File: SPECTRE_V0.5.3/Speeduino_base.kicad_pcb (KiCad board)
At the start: 2 copper layers, 100 x 93 mm, 218 parts, among them J1 Conn_01x06_Male, J2 Conn_02x04_Odd_Even, J3 ProtoArea, Q1 AO3400, Q10 BSP78, Q11 BSP78, Q12 AO3400, Q13 BSP78, Q14 BSP78, Q15 BSP78, Q16 BSP78, Q17 BSP78, Q18 BSP78, Q19 BSP78, Q20 BSP78, Q21 BSP78, Q6 AO3400, Q7 AO3400, U1 MAX9926UAEE+, U10 MIC4427, U2 LM78M05_TO220, U3 TL431DBZ, U4 molex_48pin, U5 TJA1050, U6 MAX3232, U7 MIC4427, U8 MIC4427, U9 MIC4427

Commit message: more cleanup after changing molex 48pin
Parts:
- U4: footprint rusefi_lib:Molex_48 -> Speeduino_base:Molex_48
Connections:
- JP13 pad 1: CANH -> Net-(JP13-Pad1)
- JP13 pad 2: Net-(JP13-Pad2) -> CANH
- R25 pad 1: PC2 -> Net-(C11-Pad2)
- R25 pad 2: Net-(C11-Pad2) -> PC2
- R28 pad 1: PC4 -> Net-(C14-Pad2)
- R28 pad 2: Net-(C14-Pad2) -> PC4
- R46 pad 1: PB1 -> Net-(C20-Pad2)
- R46 pad 2: Net-(C20-Pad2) -> PB1
- R66 pad 1: Net-(Q7-Pad1) -> PWR_GND
- R66 pad 2: PWR_GND -> Net-(Q7-Pad1)
- R67 pad 1: Net-(Q7-Pad1) -> PC13
- R67 pad 2: PC13 -> Net-(Q7-Pad1)
- R74 pad 1: Net-(JP13-Pad2) -> Net-(JP13-Pad1)
- R83 pad 1: PD3 -> PC7
- R86 pad 1: Net-(Q15-Pad1) -> PWR_GND
- R86 pad 2: PWR_GND -> Net-(Q15-Pad1)
- R87 pad 1: Net-(Q16-Pad1) -> PWR_GND
- R87 pad 2: PWR_GND -> Net-(Q16-Pad1)
- R88 pad 1: Net-(Q17-Pad1) -> PWR_GND
- R88 pad 2: PWR_GND -> Net-(Q17-Pad1)
- R9 pad 1: PA4 -> Net-(C3-Pad2)
- R9 pad 2: Net-(C3-Pad2) -> PA4
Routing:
- net PWR_GND: vias 98 -> 97
- net GND: vias 159 -> 158
- net (no net): vias 0 -> 2

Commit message: cleaning up board
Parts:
- moved D24 2.17 mm to (132.6, 101.6)
- moved R64 0.51 mm to (130.0, 102.6)
- moved JP15 0.25 mm to (163.1, 105.7)
- turned R66 to 180 degrees
- turned R67 to 0 degrees
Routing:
- net BOOT0_EXT: track 0.00 -> 48.9 mm, vias 0 -> 2
- net 3.3V: track 496.5 -> 508.9 mm
- net FLEX_FUEL_IN: track 0.00 -> 6.42 mm
- net Net-(JP15-Pad2): track 82.3 -> 87.9 mm
- net BOOT0: track 8.76 -> 13.0 mm
- net PE0: track 68.0 -> 70.4 mm
- net GND: track 706.9 -> 705.8 mm
- net Net-(D23-Pad3): track 44.6 -> 44.1 mm

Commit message: Done re-routing
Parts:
- moved R71 41.4 mm to (193.8, 46.2), turned to 90 degrees
- moved R70 41.2 mm to (196.6, 46.2), turned to 90 degrees
- moved R58 0.25 mm to (165.1, 77.5)
- turned JP13 to 180 degrees
- turned R25 to 0 degrees
- turned R28 to 180 degrees
- turned R46 to 90 degrees
- turned R86 to 180 degrees
- turned R87 to 0 degrees
- turned R88 to 0 degrees
- turned R9 to 270 degrees
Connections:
- R83 pad 1: PC7 -> PD3
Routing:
- net 3.3V: track 508.9 -> 525.6 mm, vias 14 -> 16
- net Spare_2-Out: track 25.4 -> 12.8 mm
- net Spare_1-Out: track 24.8 -> 13.6 mm
- net Net-(R70-Pad2): track 0.00 -> 10.8 mm
- net Net-(R71-Pad2): track 0.00 -> 8.02 mm
- net GND: track 705.8 -> 700.3 mm, vias 158 -> 159
- net PD3: track 36.4 -> 39.5 mm
- net Net-(JP13-Pad1): track 0.00 -> 2.00 mm
- net Net-(JP13-Pad2): track 1.99 -> 0.00 mm
- net PA10: track 73.0 -> 71.4 mm
- net PE1: track 85.0 -> 85.8 mm
- net Net-(R58-Pad2): track 3.95 -> 4.70 mm
- net IGN4-OUT: track 36.0 -> 36.6 mm
- net PWR_GND: vias 97 -> 99

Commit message: Clean-up board
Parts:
- moved JP15 2.29 mm to (165.4, 105.7)
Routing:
- net FLEX_FUEL_IN: track 6.42 -> 11.6 mm
- net Net-(JP15-Pad2): track 87.9 -> 90.8 mm
- net BOOT0_EXT: track 48.9 -> 50.8 mm
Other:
- board text removed: "BOOT1"

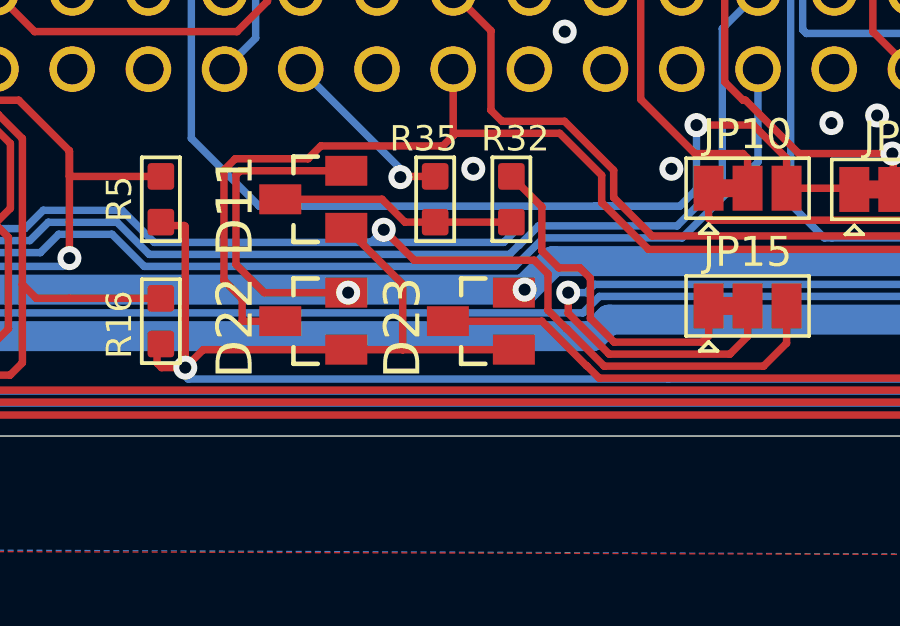
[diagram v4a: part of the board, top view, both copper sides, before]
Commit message: Update Canbus interface
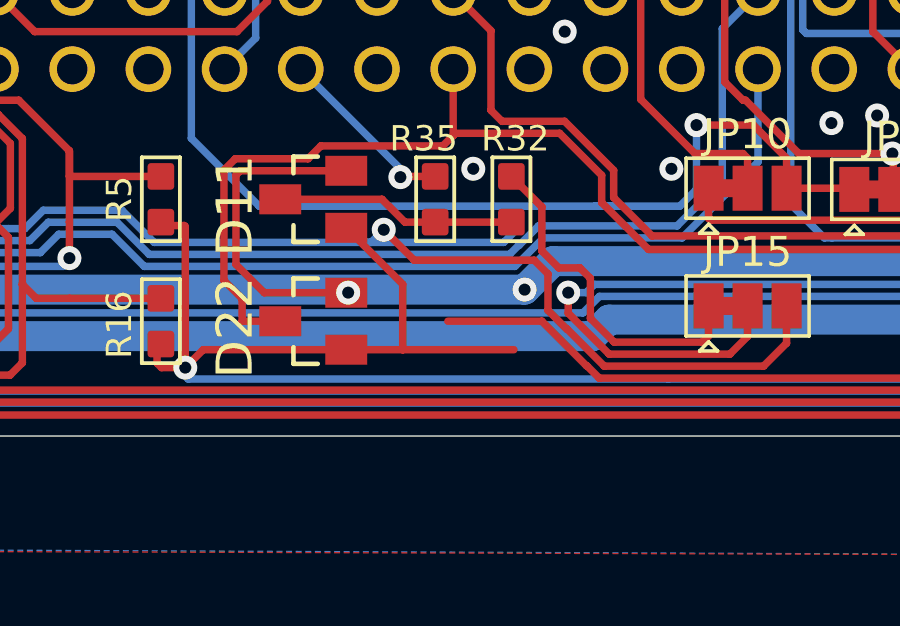
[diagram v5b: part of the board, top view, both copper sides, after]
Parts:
- removed D23: BAT54S, Speeduino_base:SOT23

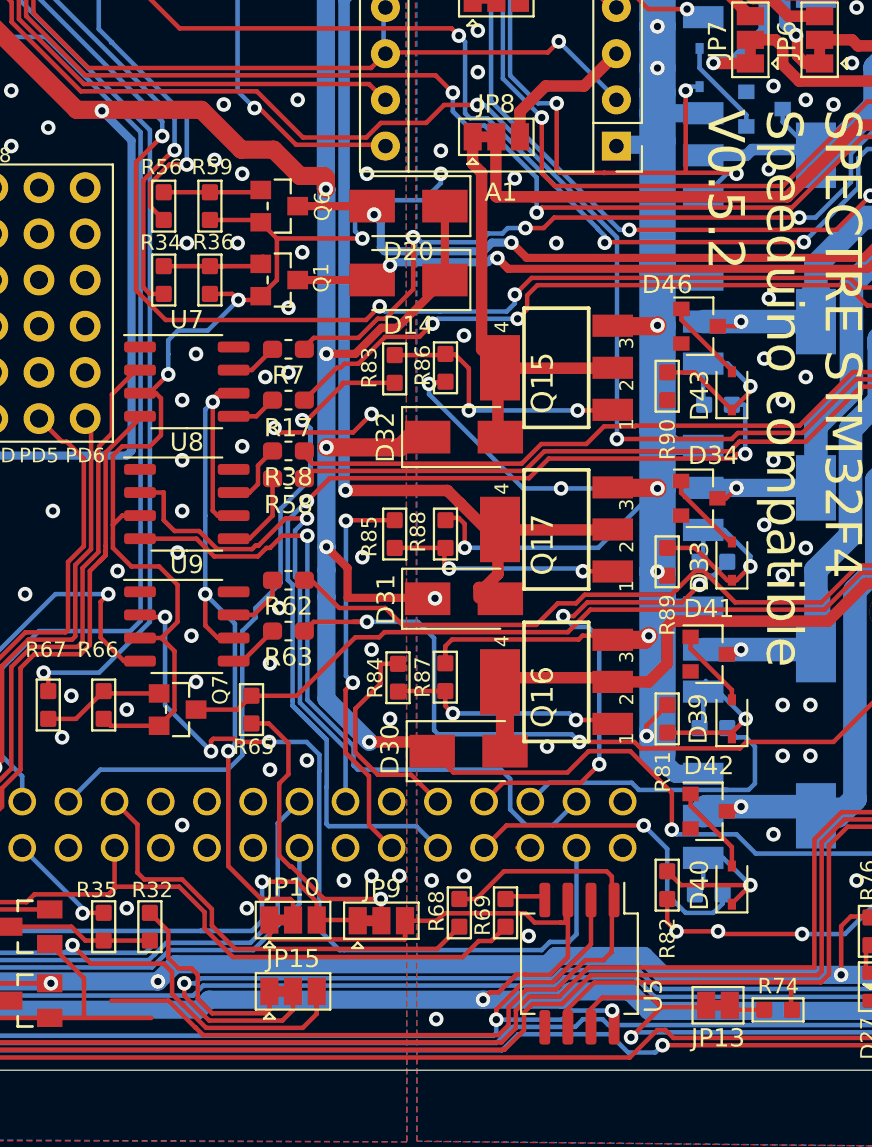
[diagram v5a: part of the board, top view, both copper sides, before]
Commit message: Update V0.5.3 Update JLCpcb part numbers in schematic Updated board layout. Added bom for JLCPCB SMT service Added location file for JLCPCB SMT service
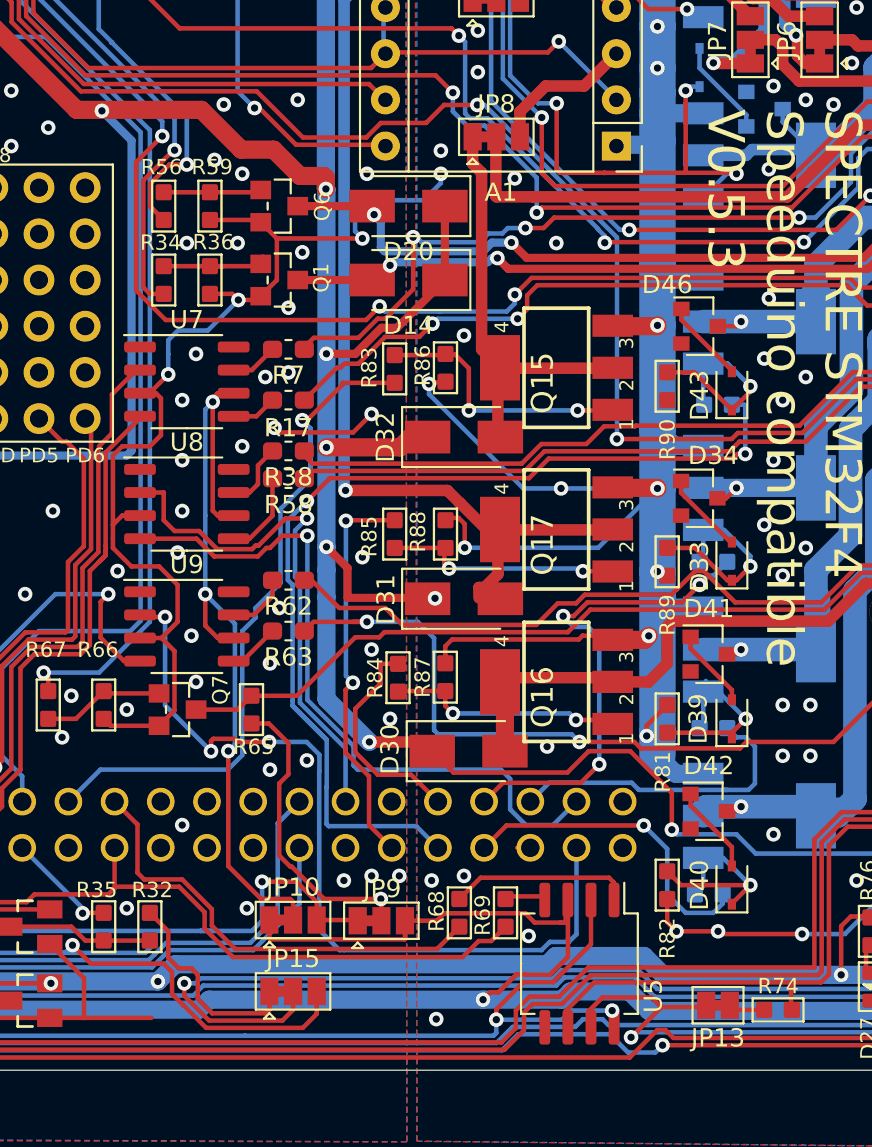
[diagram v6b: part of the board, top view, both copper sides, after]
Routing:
- net Net-(R68-Pad2): track 44.1 -> 10.1 mm
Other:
- board text added: "SPECTRE STM32F4 Speeduino compatible V0.5.3"
- board text removed: "SPECTRE STM32F4 Speeduino compatible V0.5.2"
